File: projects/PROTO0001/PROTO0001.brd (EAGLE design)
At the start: 10 parts, among them U1 PIC24FJ256GB406

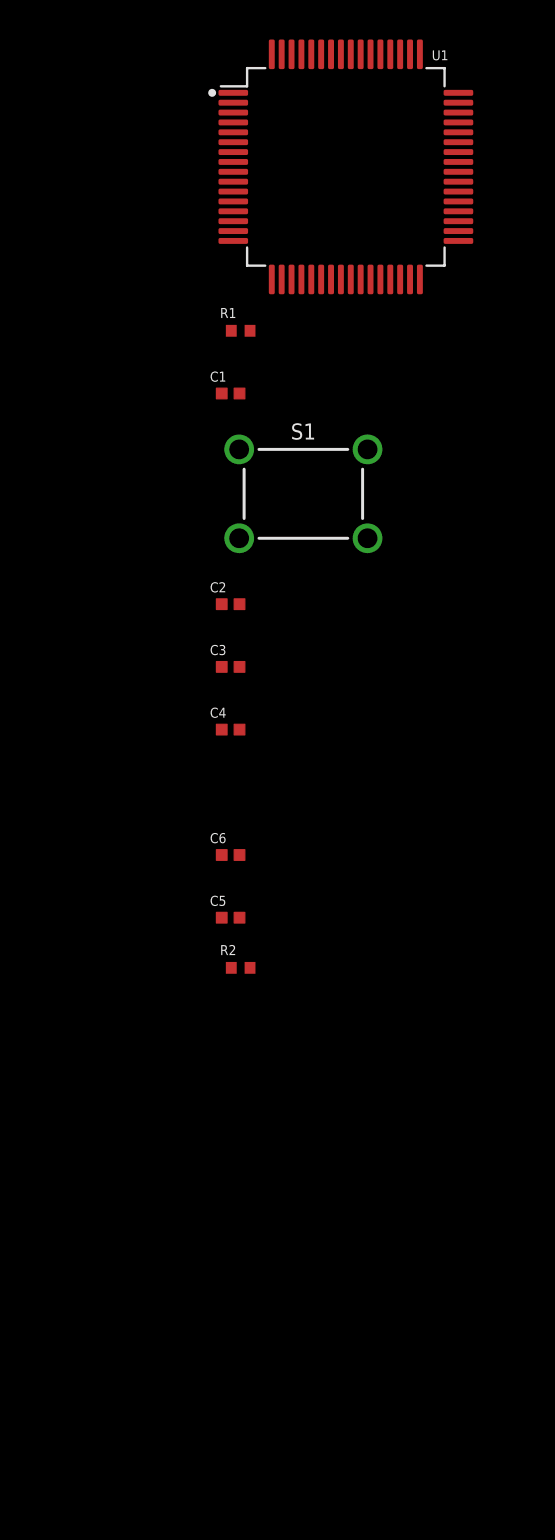
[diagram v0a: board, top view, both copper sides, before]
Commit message: Added i2c peripherals (accelerometer and HR/oximeter)
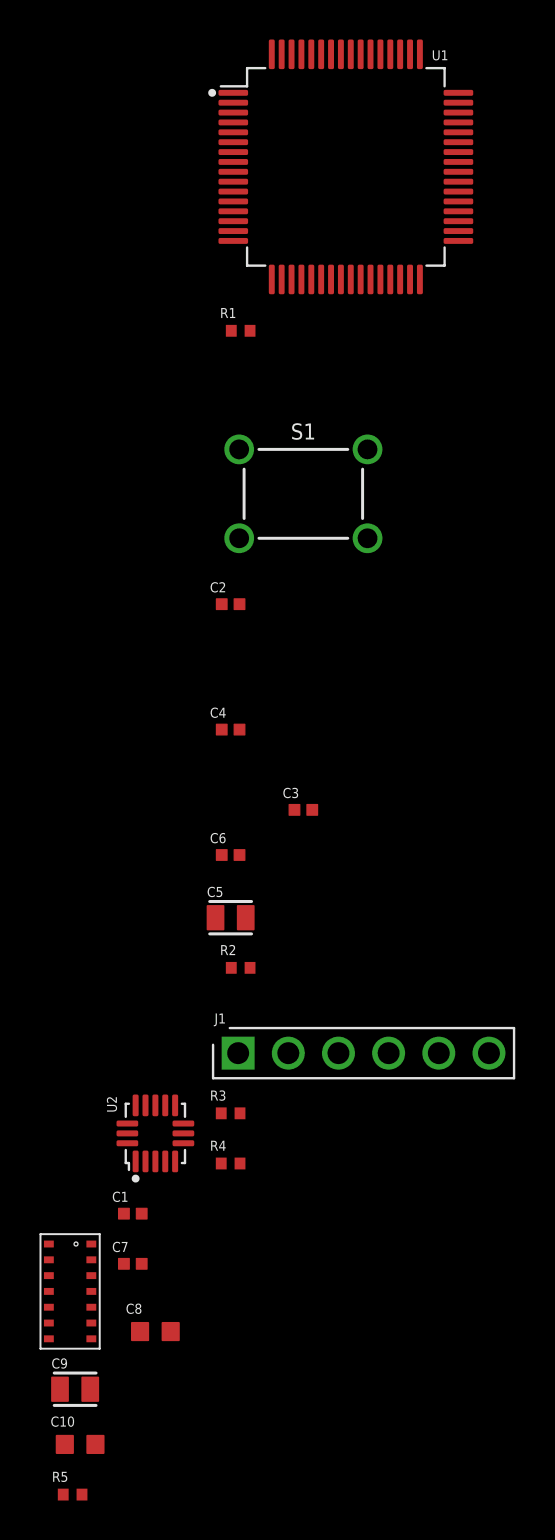
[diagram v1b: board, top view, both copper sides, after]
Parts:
- added C10: CAP_1U_0603_CERAMIC, CattleFit:CAPACITOR_0603
- added C7: CAP_100N_0402_CERAMIC, CattleFit:CAPACITOR_0402
- added C8: (no value), CattleFit:CAPACITOR_0603
- added C9: CAP_10U_0805_CERAMIC, CattleFit:CAPACITOR_0805
- added J1: (no value), CattleFit:HEADER_2.54MM_1X6
- added R3, R4, R5: (no value), CattleFit:RESISTOR_0402
- added U2: MMA8452Q, CattleFit:QFN50P300X300X100-16
- added U3: MAX30100, CattleFit:21-0880
- C5: value CAP_100N_0402_CERAMIC -> CAP_10U_0805_CERAMIC; device CattleFit:CAPACITOR_0402 -> CattleFit:CAPACITOR_0805
- moved C1 41.8 mm to (21.5, -13.0)
- moved C3 8.12 mm to (30.1, 7.49)
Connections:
- removed net MCU_AVDD: C6.1, U1.19
- removed net MCU_AVSS: C6.2, U1.20
- removed net MCU_VDD: C2.1, C3.1, U1.10, U1.26, U1.38
- new net !HR_INT: R5.1, U3.13
- new net 1V8: C10.1, U3.11
- new net 3V3: C9.1, U3.10, U3.9
- new net 5V0: C2.1, C3.1, C6.1, C7.1, C8.1, R3.2, R4.2, R5.2, U1.10, U1.19, U1.26, U1.38, U1.57, U2.1, U2.14
- new net ACC_INT1: U2.11
- new net ACC_INT2: U2.9
- new net I2C_SCL: R3.1, U1.3, U2.4, U3.2
- new net I2C_SDA: R4.1, U1.2, U2.6, U3.3
- new net PGEC: J1.5, U1.15
- new net PGED: J1.4, U1.16
- new net VUNREGULATED: J1.2
- net GND: now also C10.2, C2.2, C3.2, C4.2, C6.2, C7.2, C8.2, C9.2, J1.3, S1.3, S1.4, U1.20, U1.25, U1.41, U1.9, U2.12, U2.5, U2.7, U3.12, U3.4
- net MCU_VSS: no longer C2.2, C3.2, C4.2, U1.25, U1.41, U1.9
- net N$1: now also U2.2; no longer S1.3, S1.4
- net N$2: now also J1.1
